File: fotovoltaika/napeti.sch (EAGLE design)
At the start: 6 parts

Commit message: upravy desek
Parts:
- removed JP1: (no value), jumper:JP2E
- removed SL2: (no value), con-amp-quick:M04
- removed SL3, SL4, SL5: (no value), con-amp-quick:M03
- added ADC11150X48, ADC11150X49: (no value), con-amp-quick:M10
- added R1, R3, R5: 10k, rcl:R-EU_0204/7
- added R2: 2k7, rcl:R-EU_0204/7
- added R4, R6: 4k7, rcl:R-EU_0204/7
- added R7, R8: (no value), rcl:R-EU_0204/7
- added X1, X2, X3, X4: (no value), con-wago-500:W237-102
- SL1: device con-amp-quick:M10 -> con-amp-quick:M04
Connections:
- removed net +5V: JP1.1, SL1.10, SL2.1, SL3.2, SL4.2, SL5.2
- removed net N$11: SL1.7, SL2.4
- new net 5V: ADC11150X48.10, ADC11150X49.10, ADC11150X49.6, SL1.1
- new net N$1: ADC11150X48.1, R5.2, R6.2
- new net N$10: ADC11150X49.2, R2.1, X1-2.KL
- new net N$13: ADC11150X49.3, R3.2, R4.2
- new net N$3: ADC11150X48.2, R6.1, X3-2.KL
- new net N$4: ADC11150X48.3, R7.2, R8.2
- new net N$8: R7.1, X4-1.KL
- new net N$9: ADC11150X49.1, R1.2, R2.2
- new net SCL: ADC11150X48.5, ADC11150X48.7, ADC11150X49.7, SL1.4
- new net SDA: ADC11150X48.8, ADC11150X49.5, ADC11150X49.8, SL1.3
- net GND: now also ADC11150X48.6, ADC11150X48.9, ADC11150X49.9, SL1.2; no longer JP1.3, SL1.9, SL2.2, SL3.1, SL4.1, SL5.1
- net N$14: now also ADC11150X49.4, R4.1, X2-2.KL; no longer JP1.2, SL1.6
- net N$2: now also R1.1, X1-1.KL; no longer SL1.8, SL2.3
- net N$5: now also R3.1, X2-1.KL; no longer SL1.2, SL3.3
- net N$6: now also ADC11150X48.4, R8.1, X4-2.KL; no longer SL1.3, SL4.3
- net N$7: now also R5.1, X3-1.KL; no longer SL1.4, SL5.3

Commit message: + displej
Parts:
- renumbered ADC11150X48 to ADC11150X4A, ADC11150X49 to ADC11150X4B
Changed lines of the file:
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@@
 <?xml version="1.0" encoding="utf-8"?>
 <!DOCTYPE eagle SYSTEM "eagle.dtd">
-<eagle version="9.3.0">
+<eagle version="9.4.1">
 <drawing>
 <settings>
@@
 </classes>
 <parts>
-<part name="ADC11150X49" library="con-amp-quick" library_urn="urn:adsk.eagle:library:125" deviceset="M10" device="" package3d_urn="urn:adsk.eagle:package:5963/1"/>
-<part name="ADC11150X48" library="con-amp-quick" library_urn="urn:adsk.eagle:library:125" deviceset="M10" device="" package3d_urn="urn:adsk.eagle:package:5963/1"/>
+<part name="ADC11150X4B" library="con-amp-quick" library_urn="urn:adsk.eagle:library:125" deviceset="M10" device="" package3d_urn="urn:adsk.eagle:package:5963/1"/>
+<part name="ADC11150X4A" library="con-amp-quick" library_urn="urn:adsk.eagle:library:125" deviceset="M10" device="" package3d_urn="urn:adsk.eagle:package:5963/1"/>
 <part name="SL1" library="con-amp-quick" library_urn="urn:adsk.eagle:library:125" deviceset="M04" device="" package3d_urn="urn:adsk.eagle:package:5958/1"/>
 <part name="R1" library="rcl" library_urn="urn:adsk.eagle:library:334" deviceset="R-EU_" device="0204/7" package3d_urn="urn:adsk.eagle:package:23498/1" value="10k"/>
@@
 </plain>
 <instances>
-<instance part="ADC11150X49" gate="G$1" x="25.4" y="66.04" smashed="yes">
+<instance part="ADC11150X4B" gate="G$1" x="25.4" y="66.04" smashed="yes">
 <attribute name="VALUE" x="20.32" y="48.26" size="1.778" layer="96"/>
 <attribute name="NAME" x="20.32" y="79.502" size="1.778" layer="95"/>
 </instance>
-<instance part="ADC11150X48" gate="G$1" x="73.66" y="66.04" smashed="yes">
+<instance part="ADC11150X4A" gate="G$1" x="73.66" y="66.04" smashed="yes">
 <attribute name="VALUE" x="68.58" y="48.26" size="1.778" layer="96"/>
 <attribute name="NAME" x="68.58" y="79.502" size="1.778" layer="95"/>
@@
 <net name="5V" class="0">
 <segment>
-<pinref part="ADC11150X49" gate="G$1" pin="10"/>
+<pinref part="ADC11150X4B" gate="G$1" pin="10"/>
 <pinref part="SL1" gate="G$1" pin="1"/>
 <wire x1="30.48" y1="76.2" x2="45.72" y2="76.2" width="0.1524" layer="91"/>
 <wire x1="45.72" y1="76.2" x2="45.72" y2="83.82" width="0.1524" layer="91"/>
-<pinref part="ADC11150X48" gate="G$1" pin="10"/>
+<pinref part="ADC11150X4A" gate="G$1" pin="10"/>
 <wire x1="45.72" y1="83.82" x2="45.72" y2="86.36" width="0.1524" layer="91"/>
 <wire x1="78.74" y1="76.2" x2="83.82" y2="76.2" width="0.1524" layer="91"/>
@@
 <junction x="45.72" y="83.82"/>
 <label x="40.64" y="99.06" size="1.778" layer="95"/>
-<pinref part="ADC11150X49" gate="G$1" pin="6"/>
+<pinref part="ADC11150X4B" gate="G$1" pin="6"/>
 <wire x1="30.48" y1="66.04" x2="45.72" y2="66.04" width="0.1524" layer="91"/>
 <wire x1="45.72" y1="66.04" x2="45.72" y2="76.2" width="0.1524" layer="91"/>
@@
 <net name="GND" class="0">
 <segment>
-<pinref part="ADC11150X49" gate="G$1" pin="9"/>
+<pinref part="ADC11150X4B" gate="G$1" pin="9"/>
 <pinref part="SL1" gate="G$1" pin="2"/>
 <wire x1="30.48" y1="73.66" x2="48.26" y2="73.66" width="0.1524" layer="91"/>
 <wire x1="48.26" y1="73.66" x2="48.26" y2="81.28" width="0.1524" layer="91"/>
-<pinref part="ADC11150X48" gate="G$1" pin="9"/>
+<pinref part="ADC11150X4A" gate="G$1" pin="9"/>
 <wire x1="48.26" y1="81.28" x2="48.26" y2="86.36" width="0.1524" layer="91"/>
 <wire x1="78.74" y1="73.66" x2="81.28" y2="73.66" width="0.1524" layer="91"/>
@@
 <junction x="48.26" y="81.28"/>
 <label x="45.72" y="99.06" size="1.778" layer="95"/>
-<pinref part="ADC11150X48" gate="G$1" pin="6"/>
+<pinref part="ADC11150X4A" gate="G$1" pin="6"/>
 <wire x1="78.74" y1="66.04" x2="88.9" y2="66.04" width="0.1524" layer="91"/>
 <wire x1="88.9" y1="66.04" x2="88.9" y2="45.72" width="0.1524" layer="91"/>
@@
 <net name="SDA" class="0">
 <segment>
-<pinref part="ADC11150X49" gate="G$1" pin="8"/>
+<pinref part="ADC11150X4B" gate="G$1" pin="8"/>
 <pinref part="SL1" gate="G$1" pin="3"/>
 <wire x1="30.48" y1="71.12" x2="35.56" y2="71.12" width="0.1524" layer="91"/>
 <wire x1="35.56" y1="71.12" x2="50.8" y2="71.12" width="0.1524" layer="91"/>
 <wire x1="50.8" y1="71.12" x2="50.8" y2="86.36" width="0.1524" layer="91"/>
-<pinref part="ADC11150X48" gate="G$1" pin="8"/>
+<pinref part="ADC11150X4A" gate="G$1" pin="8"/>
 <wire x1="78.74" y1="71.12" x2="86.36" y2="71.12" width="0.1524" layer="91"/>
 <wire x1="86.36" y1="71.12" x2="86.36" y2="88.9" width="0.1524" layer="91"/>
@@
 <junction x="50.8" y="71.12"/>
 <label x="53.34" y="99.06" size="1.778" layer="95"/>
-<pinref part="ADC11150X49" gate="G$1" pin="5"/>
+<pinref part="ADC11150X4B" gate="G$1" pin="5"/>
 <wire x1="30.48" y1="63.5" x2="35.56" y2="63.5" width="0.1524" layer="91"/>
 <wire x1="35.56" y1="63.5" x2="35.56" y2="71.12" width="0.1524" layer="91"/>
@@
 <net name="SCL" class="0">
 <segment>
-<pinref part="ADC11150X49" gate="G$1" pin="7"/>
+<pinref part="ADC11150X4B" gate="G$1" pin="7"/>
 <pinref part="SL1" gate="G$1" pin="4"/>
 <wire x1="30.48" y1="68.58" x2="53.34" y2="68.58" width="0.1524" layer="91"/>
 <wire x1="53.34" y1="68.58" x2="53.34" y2="73.66" width="0.1524" layer="91"/>
-<pinref part="ADC11150X48" gate="G$1" pin="7"/>
+<pinref part="ADC11150X4A" gate="G$1" pin="7"/>
 <wire x1="53.34" y1="73.66" x2="53.34" y2="86.36" width="0.1524" layer="91"/>
 <wire x1="78.74" y1="68.58" x2="83.82" y2="68.58" width="0.1524" layer="91"/>
@@
 <junction x="53.34" y="73.66"/>
 <label x="60.96" y="99.06" size="1.778" layer="95"/>
-<pinref part="ADC11150X48" gate="G$1" pin="5"/>
+<pinref part="ADC11150X4A" gate="G$1" pin="5"/>
 <wire x1="78.74" y1="63.5" x2="83.82" y2="63.5" width="0.1524" layer="91"/>
 <wire x1="83.82" y1="63.5" x2="83.82" y2="68.58" width="0.1524" layer="91"/>
@@
 <net name="N$9" class="0">
 <segment>
-<pinref part="ADC11150X49" gate="G$1" pin="1"/>
+<pinref part="ADC11150X4B" gate="G$1" pin="1"/>
 <wire x1="30.48" y1="53.34" x2="30.48" y2="30.48" width="0.1524" layer="91"/>
 <pinref part="R1" gate="G$1" pin="2"/>
@@
 <net name="N$10" class="0">
 <segment>
-<pinref part="ADC11150X49" gate="G$1" pin="2"/>
+<pinref part="ADC11150X4B" gate="G$1" pin="2"/>
 <wire x1="30.48" y1="55.88" x2="33.02" y2="55.88" width="0.1524" layer="91"/>
 <wire x1="33.02" y1="55.88" x2="33.02" y2="33.02" width="0.1524" layer="91"/>
@@
 <net name="N$13" class="0">
 <segment>
-<pinref part="ADC11150X49" gate="G$1" pin="3"/>
+<pinref part="ADC11150X4B" gate="G$1" pin="3"/>
 <wire x1="30.48" y1="58.42" x2="35.56" y2="58.42" width="0.1524" layer="91"/>
 <wire x1="35.56" y1="58.42" x2="35.56" y2="35.56" width="0.1524" layer="91"/>
@@
 <net name="N$14" class="0">
 <segment>
-<pinref part="ADC11150X49" gate="G$1" pin="4"/>
+<pinref part="ADC11150X4B" gate="G$1" pin="4"/>
 <wire x1="30.48" y1="60.96" x2="38.1" y2="60.96" width="0.1524" layer="91"/>
 <wire x1="38.1" y1="60.96" x2="38.1" y2="40.64" width="0.1524" layer="91"/>
@@
 <pinref part="R6" gate="G$1" pin="2"/>
 <wire x1="73.66" y1="30.48" x2="78.74" y2="30.48" width="0.1524" layer="91"/>
-<pinref part="ADC11150X48" gate="G$1" pin="1"/>
+<pinref part="ADC11150X4A" gate="G$1" pin="1"/>
 <wire x1="78.74" y1="30.48" x2="81.28" y2="30.48" width="0.1524" layer="91"/>
 <wire x1="78.74" y1="53.34" x2="78.74" y2="30.48" width="0.1524" layer="91"/>
@@
 <wire x1="81.28" y1="10.16" x2="81.28" y2="20.32" width="0.1524" layer="91"/>
 <junction x="81.28" y="20.32"/>
-<pinref part="ADC11150X48" gate="G$1" pin="2"/>
+<pinref part="ADC11150X4A" gate="G$1" pin="2"/>
 <wire x1="78.74" y1="55.88" x2="86.36" y2="55.88" width="0.1524" layer="91"/>
 <wire x1="86.36" y1="55.88" x2="86.36" y2="20.32" width="0.1524" layer="91"/>
@@
 <wire x1="93.98" y1="30.48" x2="101.6" y2="30.48" width="0.1524" layer="91"/>
 <junction x="93.98" y="30.48"/>
-<pinref part="ADC11150X48" gate="G$1" pin="3"/>
+<pinref part="ADC11150X4A" gate="G$1" pin="3"/>
 <wire x1="78.74" y1="58.42" x2="93.98" y2="58.42" width="0.1524" layer="91"/>
 <wire x1="93.98" y1="58.42" x2="93.98" y2="30.48" width="0.1524" layer="91"/>
@@
 <wire x1="101.6" y1="10.16" x2="101.6" y2="20.32" width="0.1524" layer="91"/>
 <junction x="101.6" y="20.32"/>
-<pinref part="ADC11150X48" gate="G$1" pin="4"/>
+<pinref part="ADC11150X4A" gate="G$1" pin="4"/>
 <wire x1="78.74" y1="60.96" x2="106.68" y2="60.96" width="0.1524" layer="91"/>
 <wire x1="106.68" y1="60.96" x2="106.68" y2="20.32" width="0.1524" layer="91"/>

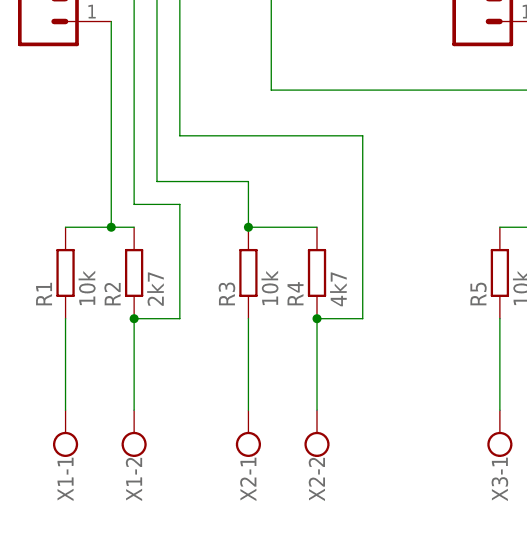
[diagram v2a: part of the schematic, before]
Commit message: prodloužení intervalu sepnutí relé na 1 hodinu dělení proudu 2, nevím proč vychází proud 2x více než ve skutečnosti je, zjistit
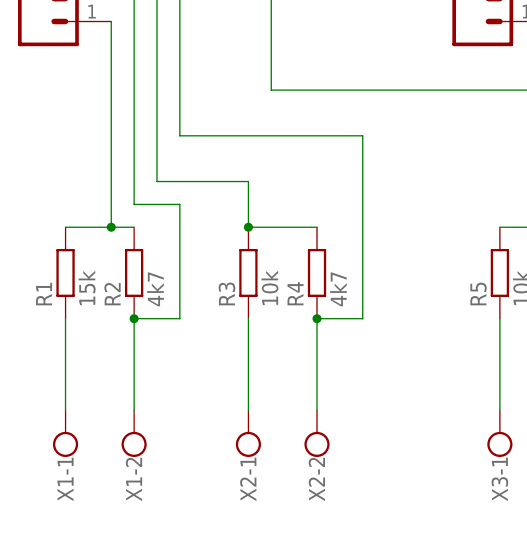
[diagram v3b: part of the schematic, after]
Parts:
- R1: value 10k -> 15k
- R2: value 2k7 -> 4k7
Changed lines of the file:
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@@
 <?xml version="1.0" encoding="utf-8"?>
 <!DOCTYPE eagle SYSTEM "eagle.dtd">
-<eagle version="9.4.1">
+<eagle version="9.4.2">
 <drawing>
 <settings>
@@
 <part name="ADC11150X4A" library="con-amp-quick" library_urn="urn:adsk.eagle:library:125" deviceset="M10" device="" package3d_urn="urn:adsk.eagle:package:5963/1"/>
 <part name="SL1" library="con-amp-quick" library_urn="urn:adsk.eagle:library:125" deviceset="M04" device="" package3d_urn="urn:adsk.eagle:package:5958/1"/>
-<part name="R1" library="rcl" library_urn="urn:adsk.eagle:library:334" deviceset="R-EU_" device="0204/7" package3d_urn="urn:adsk.eagle:package:23498/1" value="10k"/>
-<part name="R2" library="rcl" library_urn="urn:adsk.eagle:library:334" deviceset="R-EU_" device="0204/7" package3d_urn="urn:adsk.eagle:package:23498/1" value="2k7"/>
+<part name="R1" library="rcl" library_urn="urn:adsk.eagle:library:334" deviceset="R-EU_" device="0204/7" package3d_urn="urn:adsk.eagle:package:23498/1" value="15k"/>
+<part name="R2" library="rcl" library_urn="urn:adsk.eagle:library:334" deviceset="R-EU_" device="0204/7" package3d_urn="urn:adsk.eagle:package:23498/1" value="4k7"/>
 <part name="R3" library="rcl" library_urn="urn:adsk.eagle:library:334" deviceset="R-EU_" device="0204/7" package3d_urn="urn:adsk.eagle:package:23498/1" value="10k"/>
 <part name="R4" library="rcl" library_urn="urn:adsk.eagle:library:334" deviceset="R-EU_" device="0204/7" package3d_urn="urn:adsk.eagle:package:23498/1" value="4k7"/>

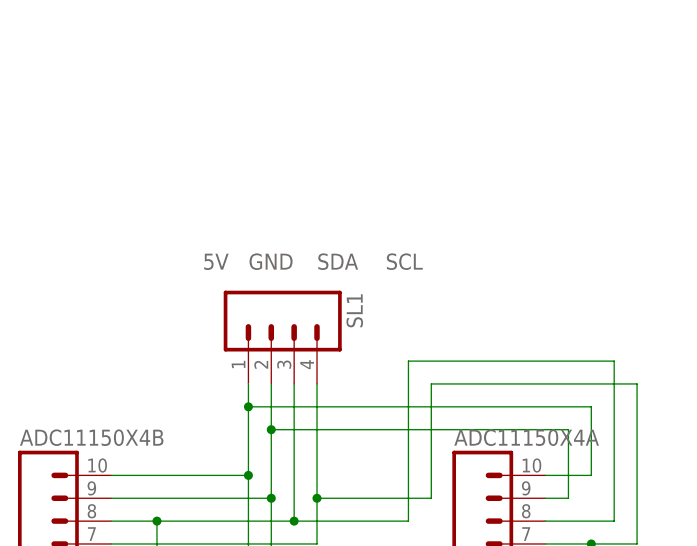
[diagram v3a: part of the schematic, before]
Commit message: uprava desky pro mereni napeti pro JST-XH konektor
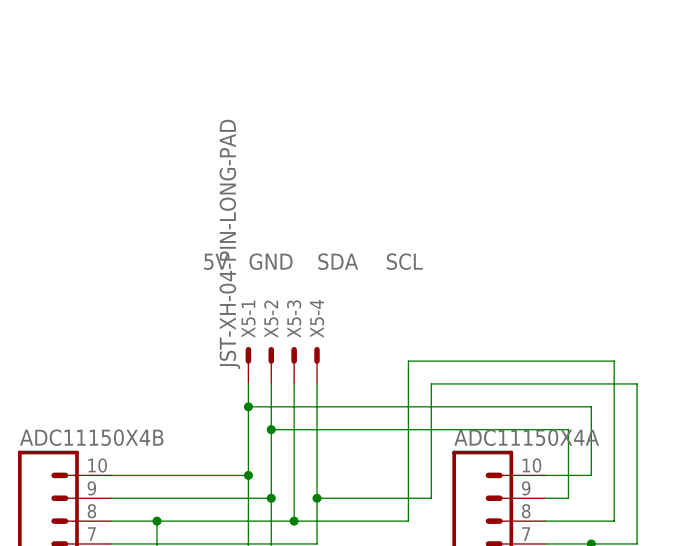
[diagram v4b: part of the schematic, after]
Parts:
- removed SL1: (no value), con-amp-quick:M04
- added X5: JST-XH-04-PIN-LONG-PAD, Rembrandt:JST-XH-04-PIN-LONG-PAD
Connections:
- net 5V: now also X5-1.S; no longer SL1.1
- net GND: now also X5-2.S; no longer SL1.2
- net SCL: now also X5-4.S; no longer SL1.4
- net SDA: now also X5-3.S; no longer SL1.3
